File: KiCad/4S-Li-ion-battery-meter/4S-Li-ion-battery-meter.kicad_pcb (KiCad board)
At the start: 2 copper layers, 45 x 12 mm, 25 parts, among them J1 Conn_01x02_Pin, SW1 SW_Push, U1 LM339

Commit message: Sent to production!
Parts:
- added G***: LOGO, TPS51386:meter, B.Cu at (152.3, 87.1)
- RV1: footprint Potentiometer_SMD:Potentiometer_Bourns_3214J_Horizontal -> Potentiometer_SMD:Potentiometer_Bourns_TC33X_Vertical
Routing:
- net Net-(R6-Pad2): track 10.3 -> 14.2 mm
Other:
- board text added: "+"
- board text added: "-"
- board text added: "4S LI-ION VOLTAGE METER V1.0"
- board text added: "G"
- board text added: "G >16.4V G >15.3V Y >14.2V Y >13.1V R <13.1V"
- board text added: "R"
- board text added: "VOLT ADJ"

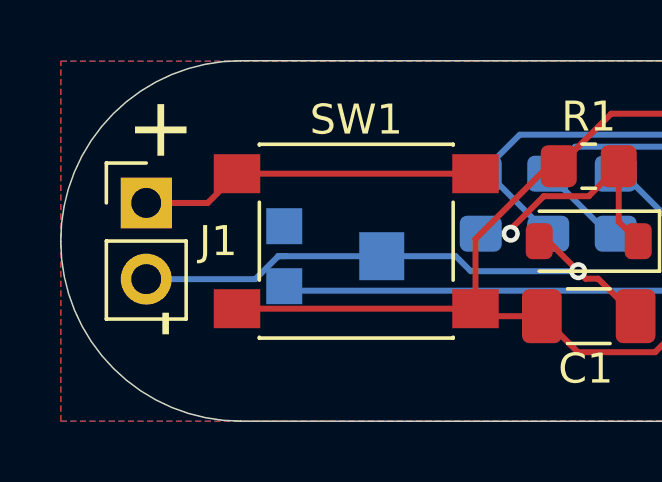
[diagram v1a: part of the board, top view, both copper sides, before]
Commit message: Fixed errors (missing enable & overlapping trace)
I should really RTFM and run the DRC...
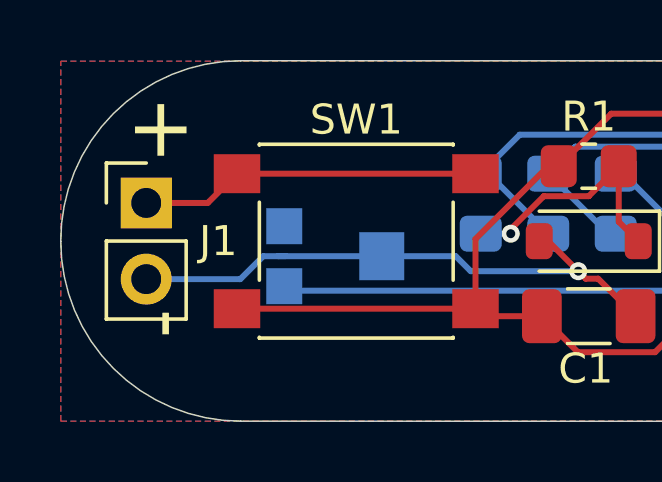
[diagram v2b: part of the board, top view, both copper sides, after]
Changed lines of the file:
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@@
 	)
 	(segment
-		(start 113.600002 88.265)
-		(end 117.235 88.265)
-		(width 0.2)
-		(layer "B.Cu")
-		(net 1)
-	)
-	(segment
-		(start 117.235 88.265)
-		(end 118 87.5)
+		(start 116.735 88.265)
+		(end 117.5 87.5)
 		(width 0.2)
 		(layer "B.Cu")
@@
 	)
 	(segment
+		(start 113.600002 88.265)
+		(end 116.735 88.265)
+		(width 0.2)
+		(layer "B.Cu")
+		(net 1)
+	)
+	(segment
 		(start 123.915257 87.5)
 		(end 124.415257 88)
 		(width 0.2)
 		(layer "B.Cu")
+		(net 1)
+	)
+	(segment
+		(start 117.5 87.5)
+		(end 118 87.5)
+		(width 0.2)
+		(layer "B.Cu")
